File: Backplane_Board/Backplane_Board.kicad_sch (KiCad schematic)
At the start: 13 parts, among them J17 Conn_01x02_Pin, Q1 AM7411P, U1 ZXTR2005ZQ-13

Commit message: ready for final schmatic review
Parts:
- removed JP1, JP3: Jumper_2_Open, symbol Jumper:Jumper_2_Open
- added J38, J39: XT60, Connector_AMASS:AMASS_XT60-F_1x02_P7.20mm_Vertical, symbol Connector:Conn_01x02_Socket
- C4, C5: footprint (none) -> EEV-TG2A331M:CAP_EEVTG2A331M
- U1: footprint (none) -> ZXTR2005ZQ-13:SOT-89_4P5X2P45_DIO-M
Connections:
- net 60V: now also J38.1 (Pin_1)
- net SHUNT+: now also J38.2 (Pin_2), J39.1 (Pin_1)
- net at J17.1 (Pin_1), Q1.1 (D): now also J39.2 (Pin_2)

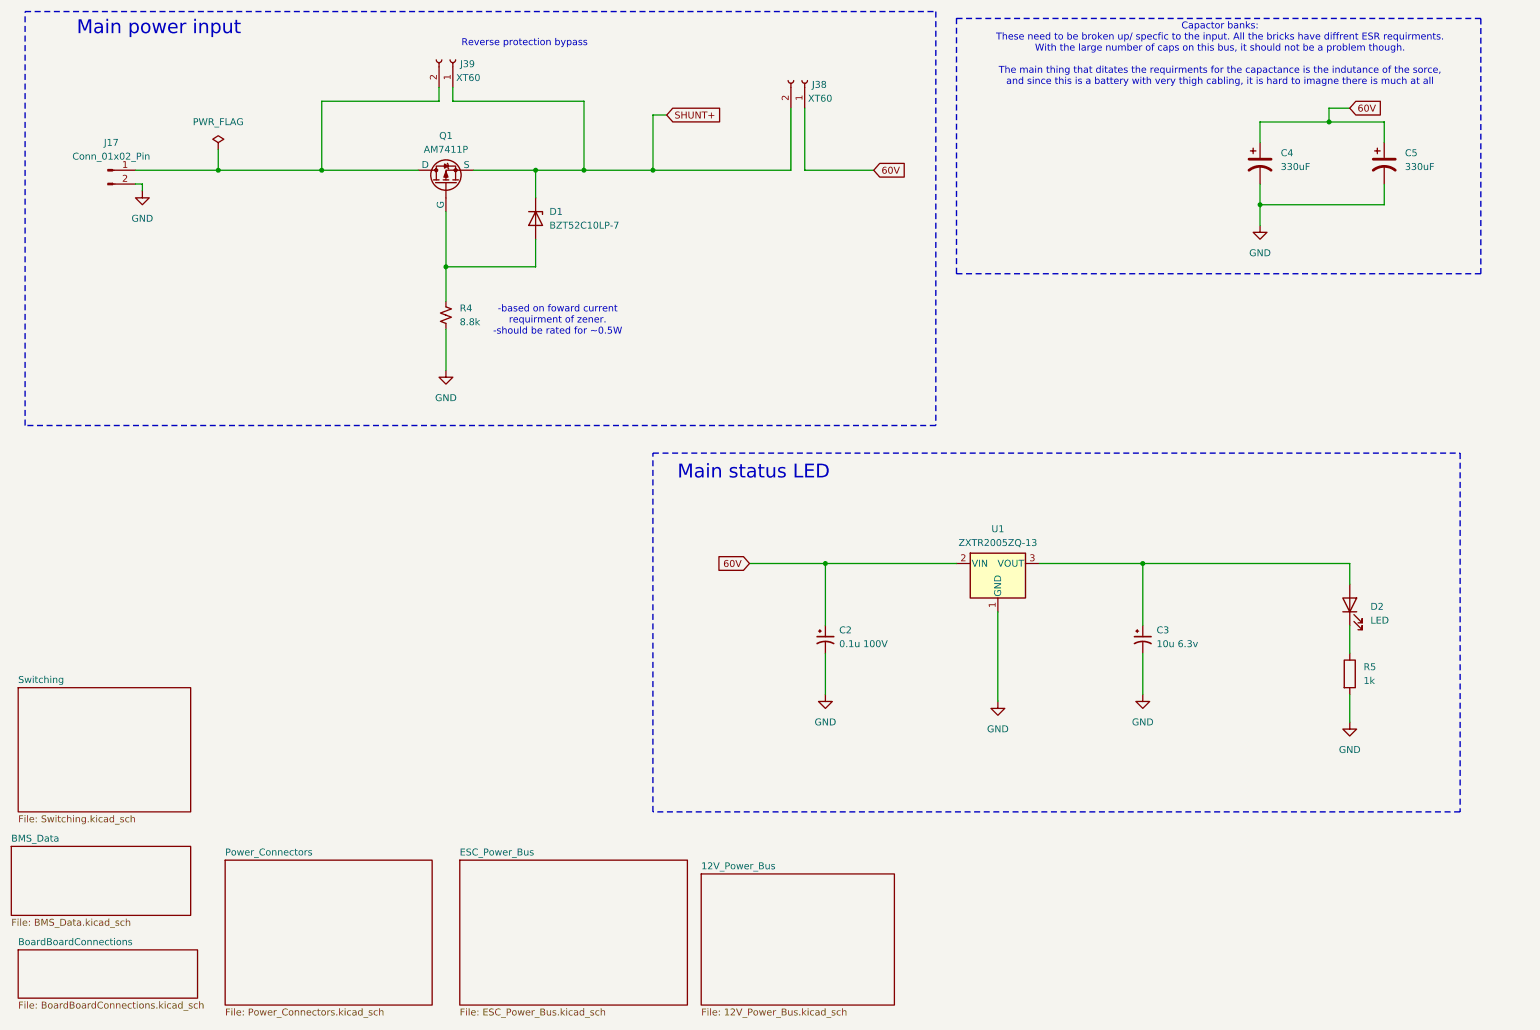
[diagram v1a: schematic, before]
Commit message: update FET circits
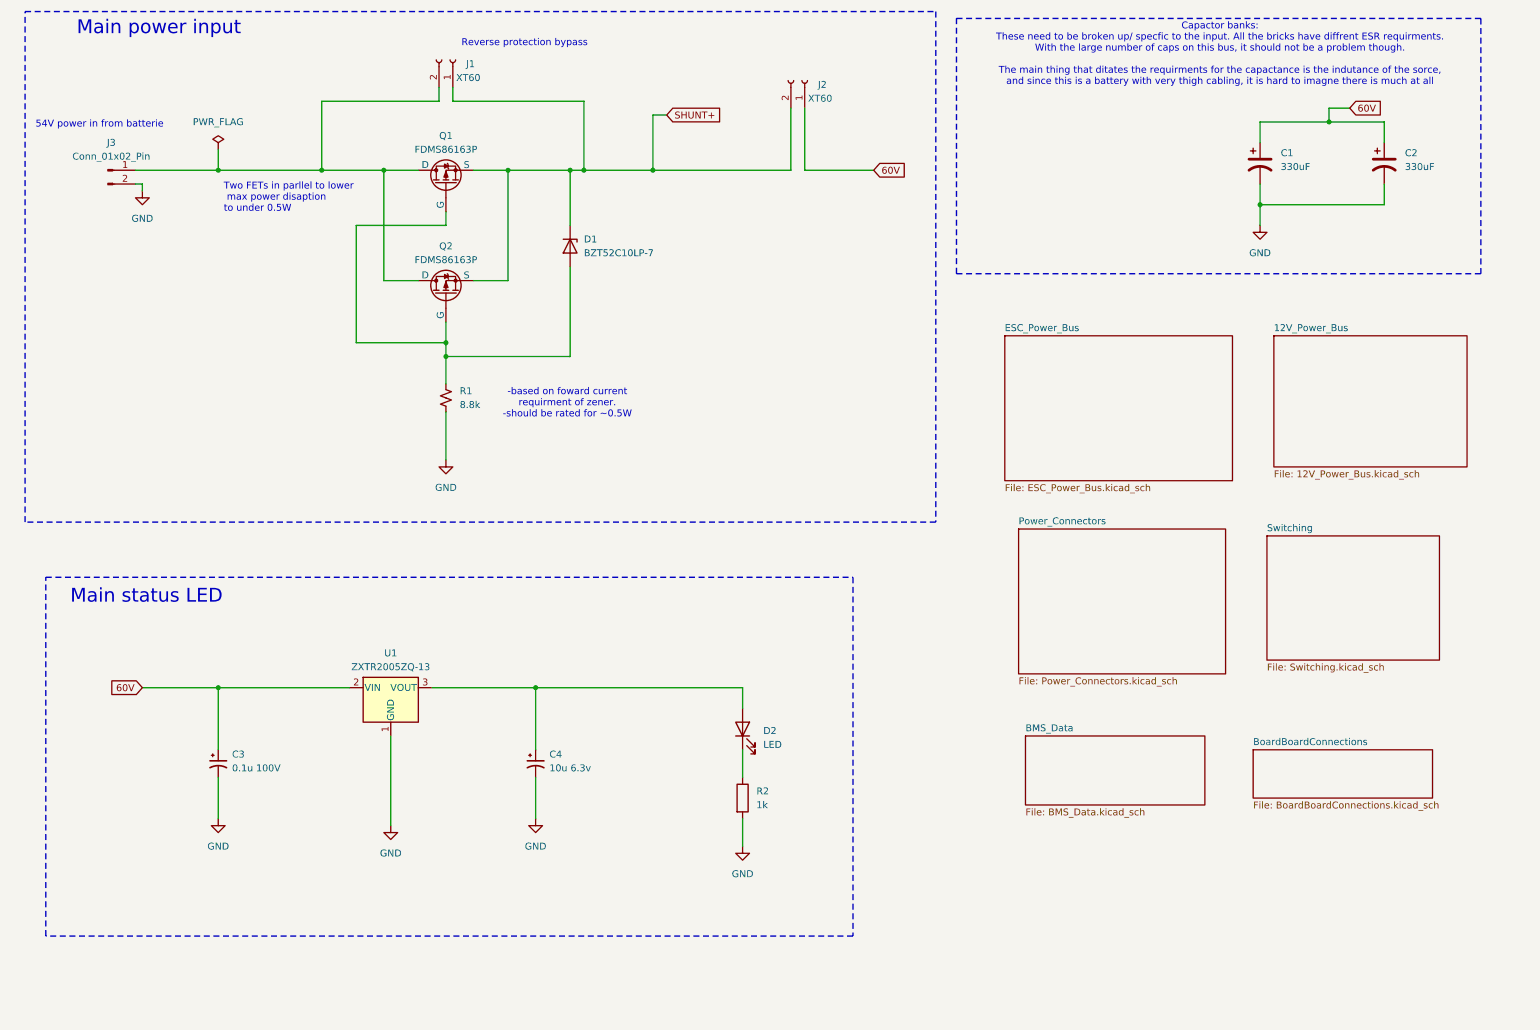
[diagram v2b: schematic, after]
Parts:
- removed C2: 0.1u 100V, symbol Device:C_Polarized_Small_US
- removed R5: 1k, symbol Device:R
- added C4: 10u 6.3v, symbol Device:C_Polarized_Small_US
- added Q2: FDMS86163P, FDMS86163P:FDMS86163P, symbol Simulation_SPICE:PMOS
- added R2: 1k, symbol Device:R
- C3: value 10u 6.3v -> 0.1u 100V
- D1: footprint (none) -> Diode_SMD:D_SOD-882
- Q1: value AM7411P -> FDMS86163P; footprint (none) -> FDMS86163P:FDMS86163P
- renumbered C4 to C1, C5 to C2, J39 to J1, J38 to J2, J17 to J3, R4 to R1
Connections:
- net 60V: now also C3.1
- net GND: now also C4.2, R2.2
- net SHUNT+: now also Q2.3 (S)
- net at D2.1 (K): now also R2.1
- net at D2.2 (A), U1.3 (VOUT): now also C4.1; no longer C3.1
- net at J1.2 (Pin_2), J3.1 (Pin_1), Q1.1 (D): now also Q2.1 (D)
- net at D1.2 (A), Q1.2 (G), R1.1: now also Q2.2 (G)
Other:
- note added: "54V power in from batterie"
- note added: "Two FETs in parllel to lower max power disaption to under 0.5W"
- moved on the sheet: D1, R1

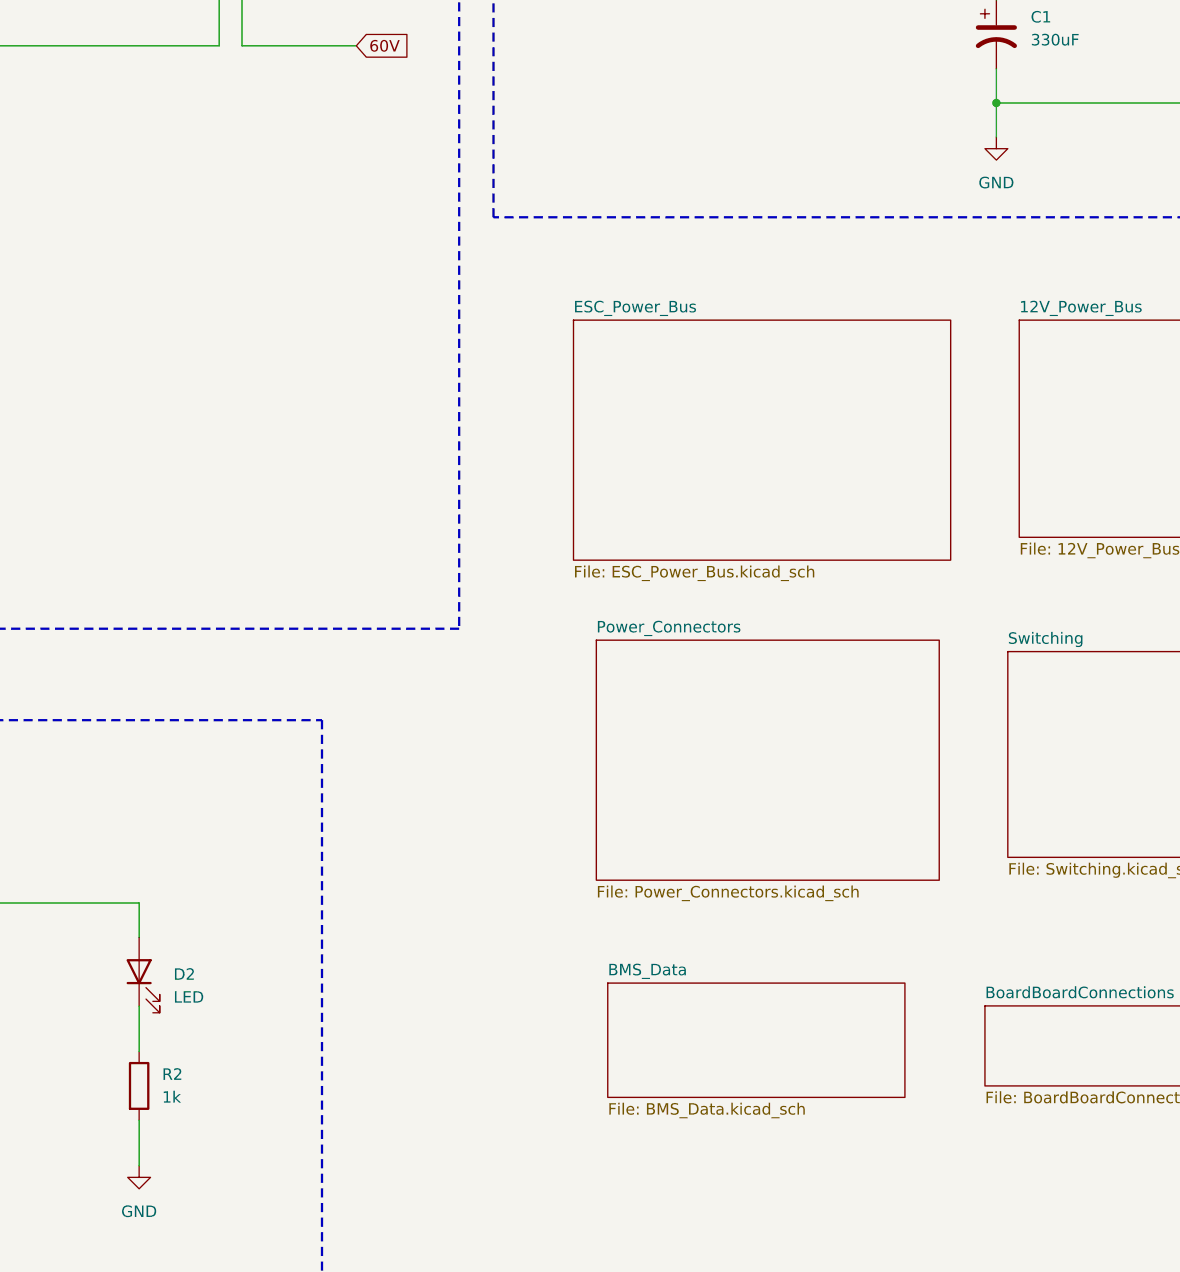
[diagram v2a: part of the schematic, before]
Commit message: adding more footprints
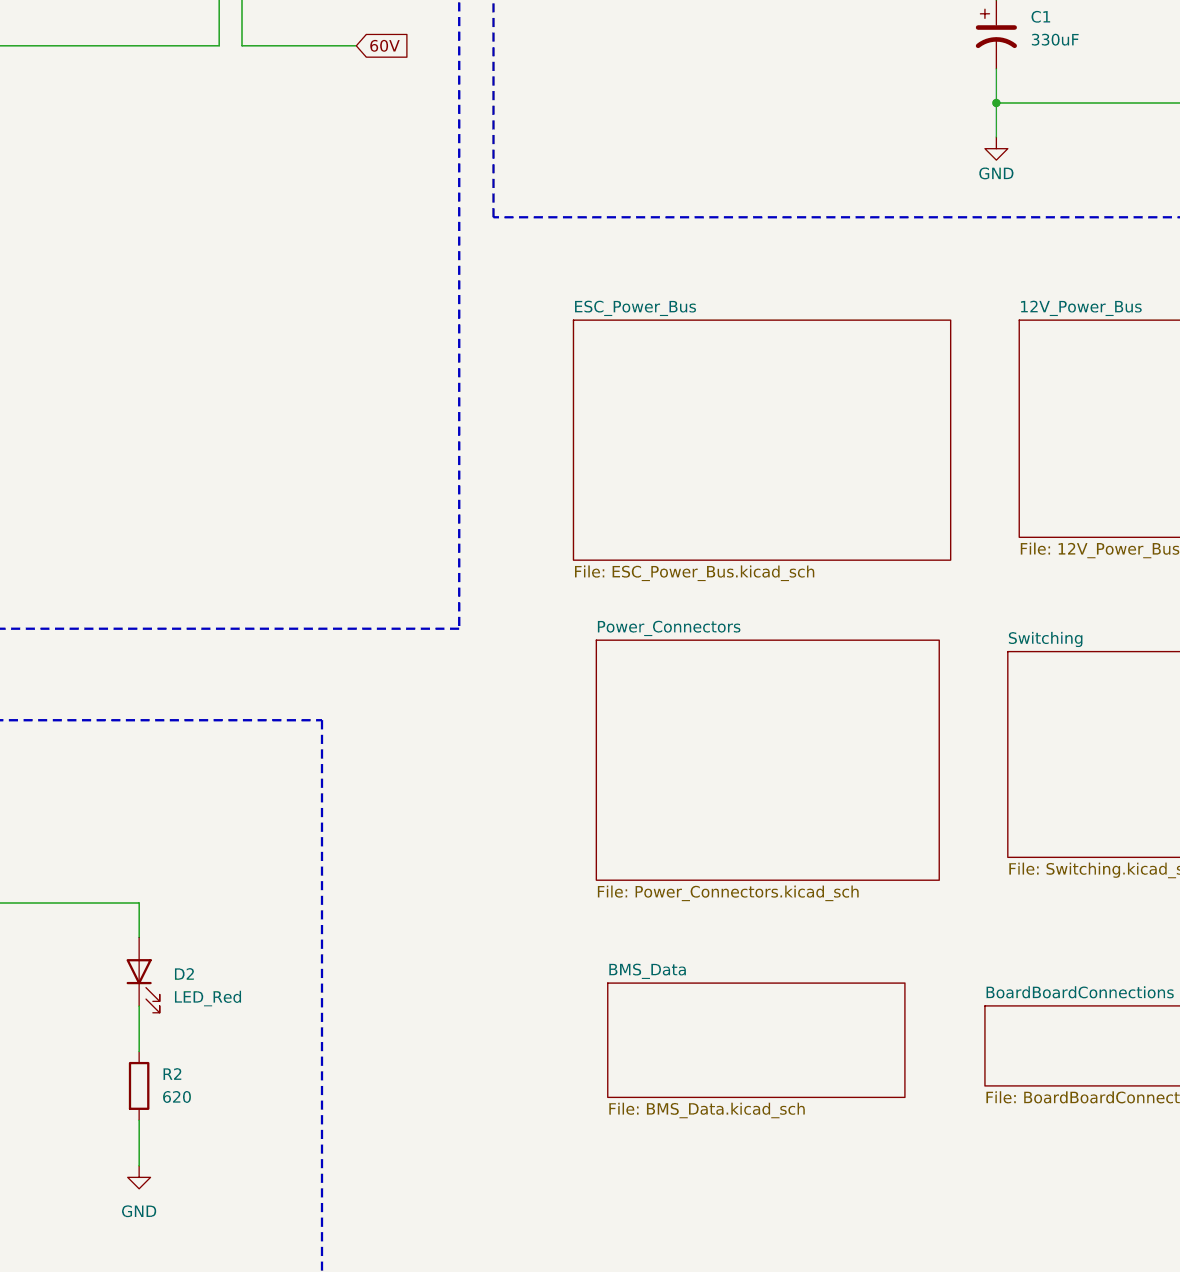
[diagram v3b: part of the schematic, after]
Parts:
- C3, C4: footprint (none) -> Capacitor_SMD:C_1206_3216Metric_Pad1.33x1.80mm_HandSolder
- D2: value LED -> LED_Red; footprint (none) -> LED_SMD:LED_0603_1608Metric
- J1, J2: footprint Connector_AMASS:AMASS_XT60-F_1x02_P7.20mm_Vertical -> Connector_AMASS:AMASS_XT30U-F_1x02_P5.0mm_Vertical
- J3: footprint (none) -> Connector_AMASS:AMASS_XT60-M_1x02_P7.20mm_Vertical
- R1: footprint (none) -> Resistor_SMD:R_1206_3216Metric_Pad1.30x1.75mm_HandSolder
- R2: value 1k -> 620; footprint (none) -> Resistor_SMD:R_1206_3216Metric_Pad1.30x1.75mm_HandSolder
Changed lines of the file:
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@@
 			)
 		)
-		(property "Footprint" ""
+		(property "Footprint" "Connector_AMASS:AMASS_XT60-M_1x02_P7.20mm_Vertical"
 			(at 30.48 41.91 0)
 			(effects
@@
 	)
 	(symbol
+		(lib_id "Device:LED")
+		(at 147.32 144.78 90)
+		(unit 1)
+		(exclude_from_sim no)
+		(in_bom yes)
+		(on_board yes)
+		(dnp no)
+		(fields_autoplaced yes)
+		(property "Reference" "D2"
+			(at 151.13 145.0974 90)
+			(effects
+				(font
+					(size 1.27 1.27)
+				)
+				(justify right)
+			)
+		)
+		(property "Value" "LED_Red"
+			(at 151.13 147.6374 90)
+			(effects
+				(font
+					(size 1.27 1.27)
+				)
+				(justify right)
+			)
+		)
+		(property "Footprint" "LED_SMD:LED_0603_1608Metric"
+			(at 147.32 144.78 0)
+			(effects
+				(font
+					(size 1.27 1.27)
+				)
+				(hide yes)
+			)
+		)
+		(property "Datasheet" "~"
+			(at 147.32 144.78 0)
+			(effects
+				(font
+					(size 1.27 1.27)
+				)
+				(hide yes)
+			)
+		)
+		(property "Description" ""
+			(at 147.32 144.78 0)
+			(effects
+				(font
+					(size 1.27 1.27)
+				)
+				(hide yes)
+			)
+		)
+		(pin "1"
+		)
+		(pin "2"
+		)
+		(instances
+			(project "Backplane_Board"
+				(path "/4484cfee-9e43-4cef-88b4-a8ca308542b4"
+					(reference "D2")
+					(unit 1)
+				)
+			)
+		)
+	)
+	(symbol
 		(lib_id "Device:C_Polarized_Small_US")
 		(at 50.8 151.13 0)
@@
 			)
 		)
-		(property "Footprint" ""
+		(property "Footprint" "Capacitor_SMD:C_1206_3216Metric_Pad1.33x1.80mm_HandSolder"
 			(at 50.8 151.13 0)
 			(effects
@@
 			)
 		)
-		(property "Footprint" "Connector_AMASS:AMASS_XT60-F_1x02_P7.20mm_Vertical"
+		(property "Footprint" "Connector_AMASS:AMASS_XT30U-F_1x02_P5.0mm_Vertical"
 			(at 93.98 21.59 0)
 			(effects
@@
 			)
 		)
-		(property "Value" "1k"
+		(property "Value" "620"
 			(at 149.86 158.7499 0)
 			(effects
@@
 			)
 		)
-		(property "Footprint" ""
+		(property "Footprint" "Resistor_SMD:R_1206_3216Metric_Pad1.30x1.75mm_HandSolder"
 			(at 145.542 157.48 90)
 			(effects
@@
 	)
 	(symbol
-		(lib_id "Device:LED")
-		(at 147.32 144.78 90)
-		(unit 1)
-		(exclude_from_sim no)
-		(in_bom yes)
-		(on_board yes)
-		(dnp no)
-		(fields_autoplaced yes)
-		(property "Reference" "D2"
-			(at 151.13 145.0974 90)
-			(effects
-				(font
-					(size 1.27 1.27)
-				)
-				(justify right)
-			)
-		)
-		(property "Value" "LED"
-			(at 151.13 147.6374 90)
-			(effects
-				(font
-					(size 1.27 1.27)
-				)
-				(justify right)
-			)
-		)
-		(property "Footprint" ""
-			(at 147.32 144.78 0)
-			(effects
-				(font
-					(size 1.27 1.27)
-				)
-				(hide yes)
-			)
-		)
-		(property "Datasheet" "~"
-			(at 147.32 144.78 0)
-			(effects
-				(font
-					(size 1.27 1.27)
-				)
-				(hide yes)
-			)
-		)
-		(property "Description" "Light emitting diode"
-			(at 147.32 144.78 0)
-			(effects
-				(font
-					(size 1.27 1.27)
-				)
-				(hide yes)
-			)
-		)
-		(pin "1"
-		)
-		(pin "2"
-		)
-		(instances
-			(project "Backplane_Board"
-				(path "/4484cfee-9e43-4cef-88b4-a8ca308542b4"
-					(reference "D2")
-					(unit 1)
-				)
-			)
-		)
-	)
-	(symbol
 		(lib_id "power:GND")
 		(at 82.55 162.56 0)
@@
 			)
 		)
-		(property "Footprint" ""
+		(property "Footprint" "Capacitor_SMD:C_1206_3216Metric_Pad1.33x1.80mm_HandSolder"
 			(at 109.22 151.13 0)
 			(effects
@@
 		(on_board yes)
 		(dnp no)
-		(fields_autoplaced yes)
 		(property "Reference" "#PWR02"
 			(at 242.57 58.42 0)
@@
 		)
 		(property "Value" "GND"
-			(at 242.57 57.15 0)
+			(at 242.57 56.134 0)
 			(effects
 				(font
@@
 			)
 		)
-		(property "Footprint" ""
+		(property "Footprint" "Resistor_SMD:R_1206_3216Metric_Pad1.30x1.75mm_HandSolder"
 			(at 92.71 83.82 0)
 			(effects
@@
 			)
 		)
-		(property "Footprint" "Connector_AMASS:AMASS_XT60-F_1x02_P7.20mm_Vertical"
+		(property "Footprint" "Connector_AMASS:AMASS_XT30U-F_1x02_P5.0mm_Vertical"
 			(at 158.75 25.4 0)
 			(effects

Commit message: derat nest ifcation
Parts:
- J1, J2: footprint Connector_AMASS:AMASS_XT30U-F_1x02_P5.0mm_Vertical -> Connector_Wire:SolderWire-2sqmm_1x02_P7.8mm_D2mm_OD3.9mm
- R2: footprint Resistor_SMD:R_1206_3216Metric_Pad1.30x1.75mm_HandSolder -> Resistor_SMD:R_0805_2012Metric_Pad1.20x1.40mm_HandSolder
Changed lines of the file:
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@@
 			)
 		)
-		(property "Footprint" "Connector_AMASS:AMASS_XT30U-F_1x02_P5.0mm_Vertical"
+		(property "Footprint" "Connector_Wire:SolderWire-2sqmm_1x02_P7.8mm_D2mm_OD3.9mm"
 			(at 93.98 21.59 0)
 			(effects
@@
 			)
 		)
-		(property "Footprint" "Resistor_SMD:R_1206_3216Metric_Pad1.30x1.75mm_HandSolder"
+		(property "Footprint" "Resistor_SMD:R_0805_2012Metric_Pad1.20x1.40mm_HandSolder"
 			(at 145.542 157.48 90)
 			(effects
@@
 			)
 		)
-		(property "Footprint" "Connector_AMASS:AMASS_XT30U-F_1x02_P5.0mm_Vertical"
+		(property "Footprint" "Connector_Wire:SolderWire-2sqmm_1x02_P7.8mm_D2mm_OD3.9mm"
 			(at 158.75 25.4 0)
 			(effects
